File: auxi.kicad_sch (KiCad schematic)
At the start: 45 parts

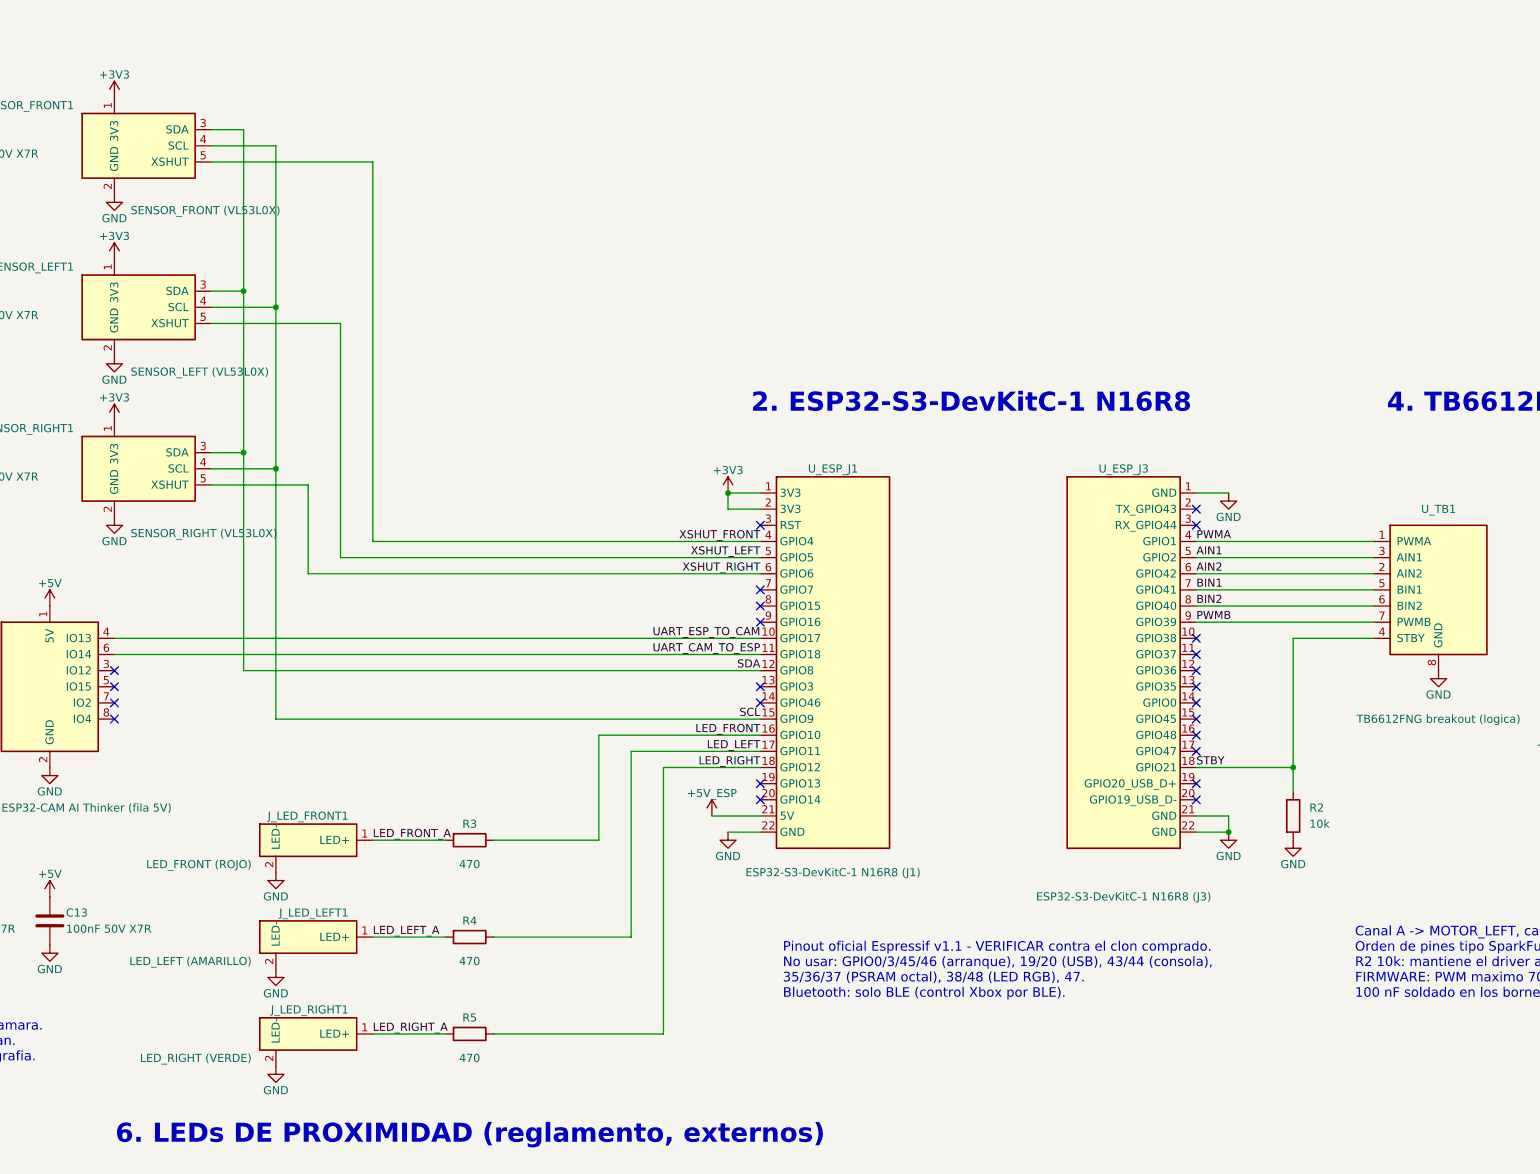
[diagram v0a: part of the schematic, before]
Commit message: feat(pcb): single-layer 110 x 140 mm board with GND pour, soldered from below
Re-do the PCB as a one-copper-layer board for home etching and hand drilling:

- Copper only on B.Cu with a GND pour; F.Cu has no copper (keepout over the
  whole top face). All parts are THT, mounted on top and soldered from below.
  No vias and no jumper wires: no two tracks cross.
- Board outline 110 x 140 mm (was 90 x 100 mm), M3 holes 5 mm from the corners,
  antenna keepouts for the ESP32-S3 and the ESP32-CAM.
- Track width >= 0.4 mm (0.3 mm only between pads / tight bundles), clearance
  0.2 mm, smallest hole 0.3 mm, default via 1.1 / 0.3 mm. Pad diameter = drill
  + 0.8 mm on every pad hole, enforced by auxi.kicad_dru. Four standard
  footprints copied into auxi.pretty with bigger pads.
- GPIOs reassigned so the signals leave the ESP32 headers in the order of their
  destinations (I2C on GPIO4/5, XSHUT 6/7/15, LEDs 8/9/10, motor signals
  reversed on J3). Schematic updated, ERC clean.
- DRC: 0 violations, 0 unconnected items.
- README.md and CLAUDE.md updated; regenerated schematic PDF, BOM, 1:1 print
  PDF (top, copper, mirrored copper) and renders.

Co-Authored-By: Claude Sonnet 5.5 <noreply@anthropic.com>
Claude-Session: https://claude.ai/code/session_01V1Casvb8MJmuQffuKiRczF
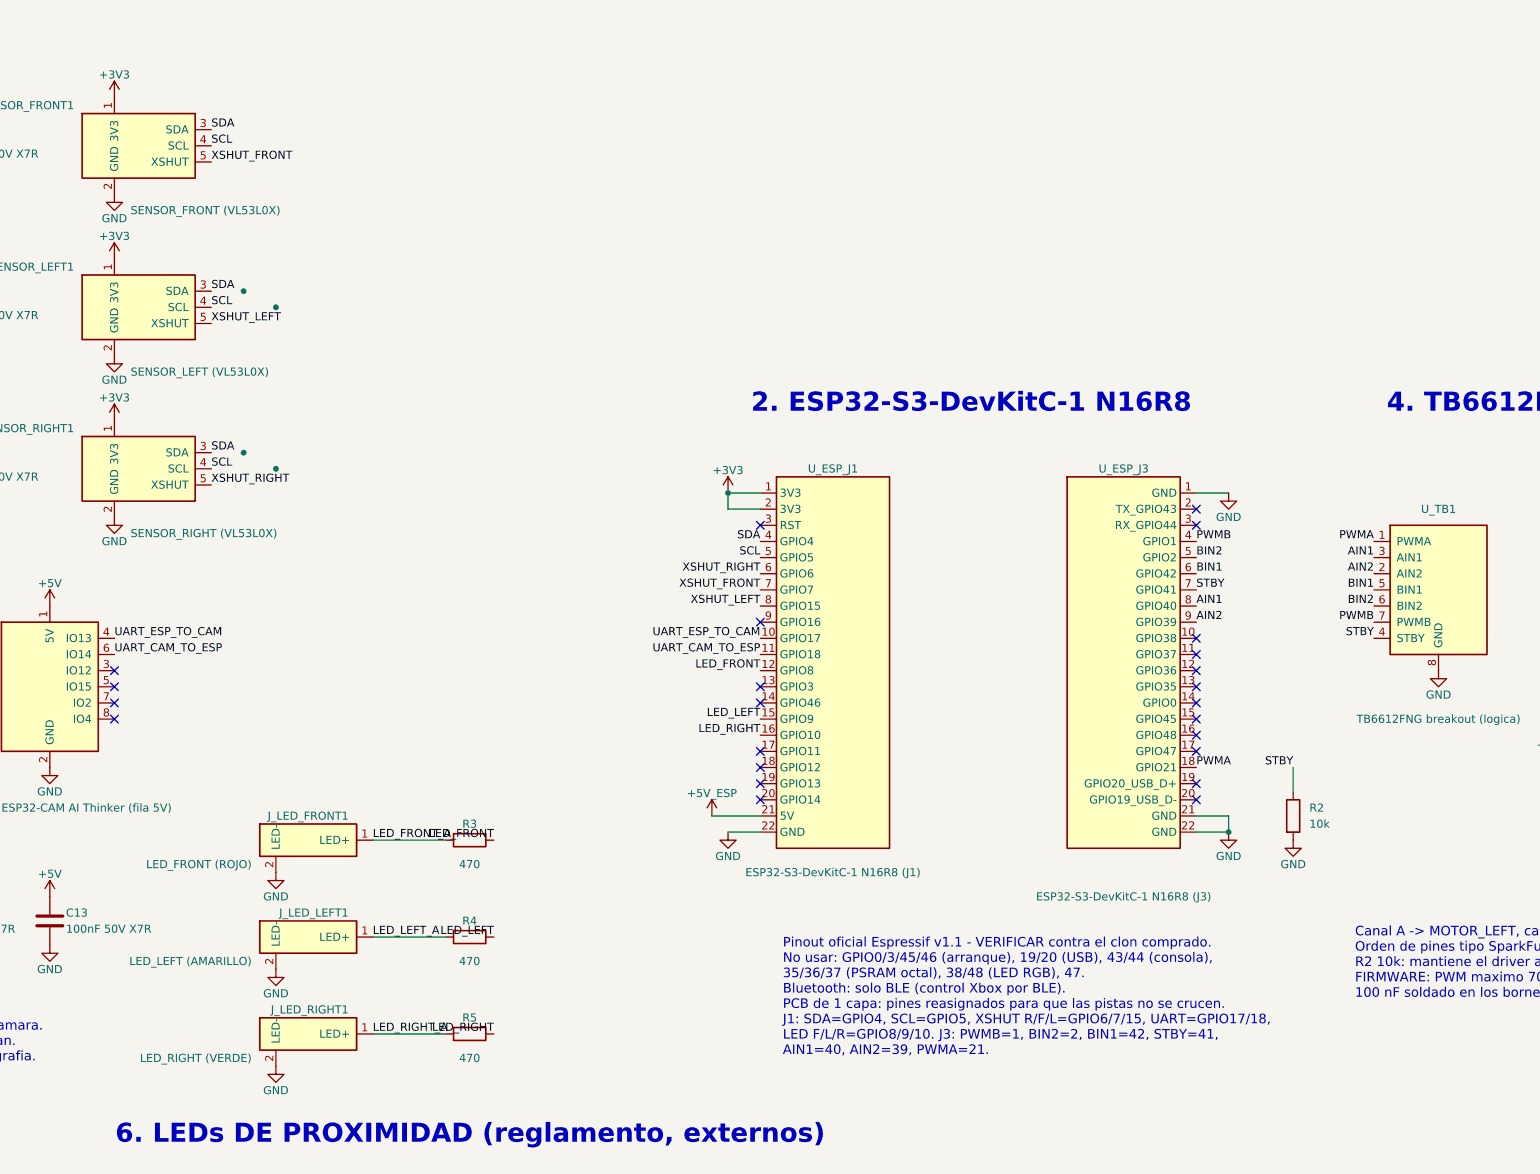
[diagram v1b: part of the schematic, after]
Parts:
- J_LED_FRONT1, J_LED_LEFT1, J_LED_POWER1, J_LED_RIGHT1: footprint Connector_PinHeader_2.54mm:PinHeader_1x02_P2.54mm_Vertical -> auxi:PinHeader_1x02_P2.54mm_Vertical
- J_SENSOR_FRONT1, J_SENSOR_LEFT1, J_SENSOR_RIGHT1: footprint Connector_JST:JST_XH_B5B-XH-A_1x05_P2.50mm_Vertical -> auxi:JST_XH_B5B-XH-A_1x05_P2.50mm_Vertical
- U_CAM1, U_CAM2, U_TB1, U_TB2: footprint Connector_PinSocket_2.54mm:PinSocket_1x08_P2.54mm_Vertical -> auxi:PinSocket_1x08_P2.54mm_Vertical
- U_ESP_J1, U_ESP_J3: footprint Connector_PinSocket_2.54mm:PinSocket_1x22_P2.54mm_Vertical -> auxi:PinSocket_1x22_P2.54mm_Vertical
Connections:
- net AIN1: now also U_ESP_J3.8 (GPIO40); no longer U_ESP_J3.5 (GPIO2)
- net AIN2: now also U_ESP_J3.9 (GPIO39); no longer U_ESP_J3.6 (GPIO42)
- net BIN1: now also U_ESP_J3.6 (GPIO42); no longer U_ESP_J3.7 (GPIO41)
- net BIN2: now also U_ESP_J3.5 (GPIO2); no longer U_ESP_J3.8 (GPIO40)
- net LED_FRONT: now also U_ESP_J1.12 (GPIO8); no longer U_ESP_J1.16 (GPIO10)
- net LED_LEFT: now also U_ESP_J1.15 (GPIO9); no longer U_ESP_J1.17 (GPIO11)
- net LED_RIGHT: now also U_ESP_J1.16 (GPIO10); no longer U_ESP_J1.18 (GPIO12)
- net PWMA: now also U_ESP_J3.18 (GPIO21); no longer U_ESP_J3.4 (GPIO1)
- net PWMB: now also U_ESP_J3.4 (GPIO1); no longer U_ESP_J3.9 (GPIO39)
- net SCL: now also U_ESP_J1.5 (GPIO5); no longer U_ESP_J1.15 (GPIO9)
- net SDA: now also U_ESP_J1.4 (GPIO4); no longer U_ESP_J1.12 (GPIO8)
- net STBY: now also U_ESP_J3.7 (GPIO41); no longer U_ESP_J3.18 (GPIO21)
- net XSHUT_FRONT: now also U_ESP_J1.7 (GPIO7); no longer U_ESP_J1.4 (GPIO4)
- net XSHUT_LEFT: now also U_ESP_J1.8 (GPIO15); no longer U_ESP_J1.5 (GPIO5)
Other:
- note added: "Pinout oficial Espressif v1.1 - VERIFICAR contra el clon comprado. No usar: GPIO0/3/45/46 (arranque), 19/20 (USB), 43/44 (consola), 35/36/37 (PSRAM octal), 38/48 (LED RGB), 47. Bluetooth: solo BLE (control Xbox por BLE). PCB de 1 capa: pines reasignados para que las pistas no se crucen. J1: SDA=GPIO4, SCL=GPIO5, XSHUT R/F/L=GPIO6/7/15, UART=GPIO17/18, LED F/L/R=GPIO8/9/10. J3: PWMB=1, BIN2=2, BIN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"
- note removed: "Pinout oficial Espressif v1.1 - VERIFICAR contra el clon comprado. No usar: GPIO0/3/45/46 (arranque), 19/20 (USB), 43/44 (consola), 35/36/37 (PSRAM octal), 38/48 (LED RGB), 47. Bluetooth: solo BLE (control Xbox por BLE)."

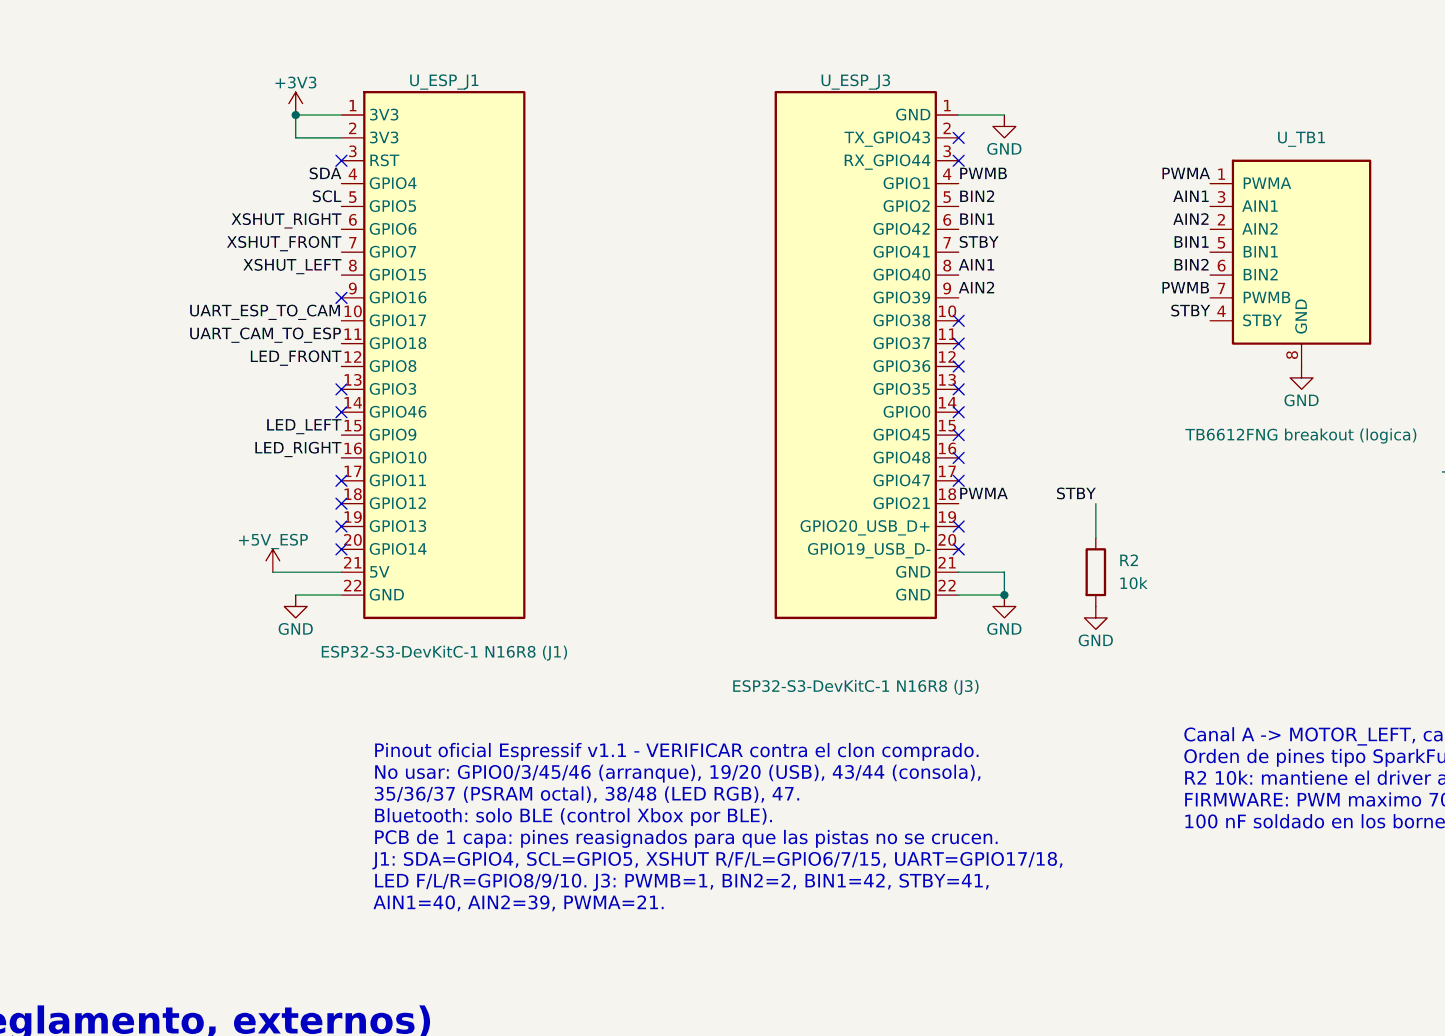
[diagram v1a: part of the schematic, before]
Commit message: Re-layout for the real orientation: 110 mm side is the front, ESP32-S3 USB at the rear edge
- ESP32-CAM at the front-left corner (camera looking forward), sensors
  along the front edge, ESP32-S3 at the rear with the USB end 1 mm from
  the edge, TB6612 and motor terminals on the east side, MP1584 on the
  west side.
- GPIO mapping changed again: XSHUT 4/5/6, SCL 7, SDA 15, UART RX 17 and
  TX 18 (schematic labels updated, ERC clean, PCB nets match the schematic).
- Board re-routed on one layer: 197 tracks, DRC 0 errors, 0 unconnected.
- README, CLAUDE.md, PDFs, renders and DRC report regenerated.

Co-Authored-By: Claude Sonnet 5.5 <noreply@anthropic.com>
Claude-Session: https://claude.ai/code/session_01V1Casvb8MJmuQffuKiRczF
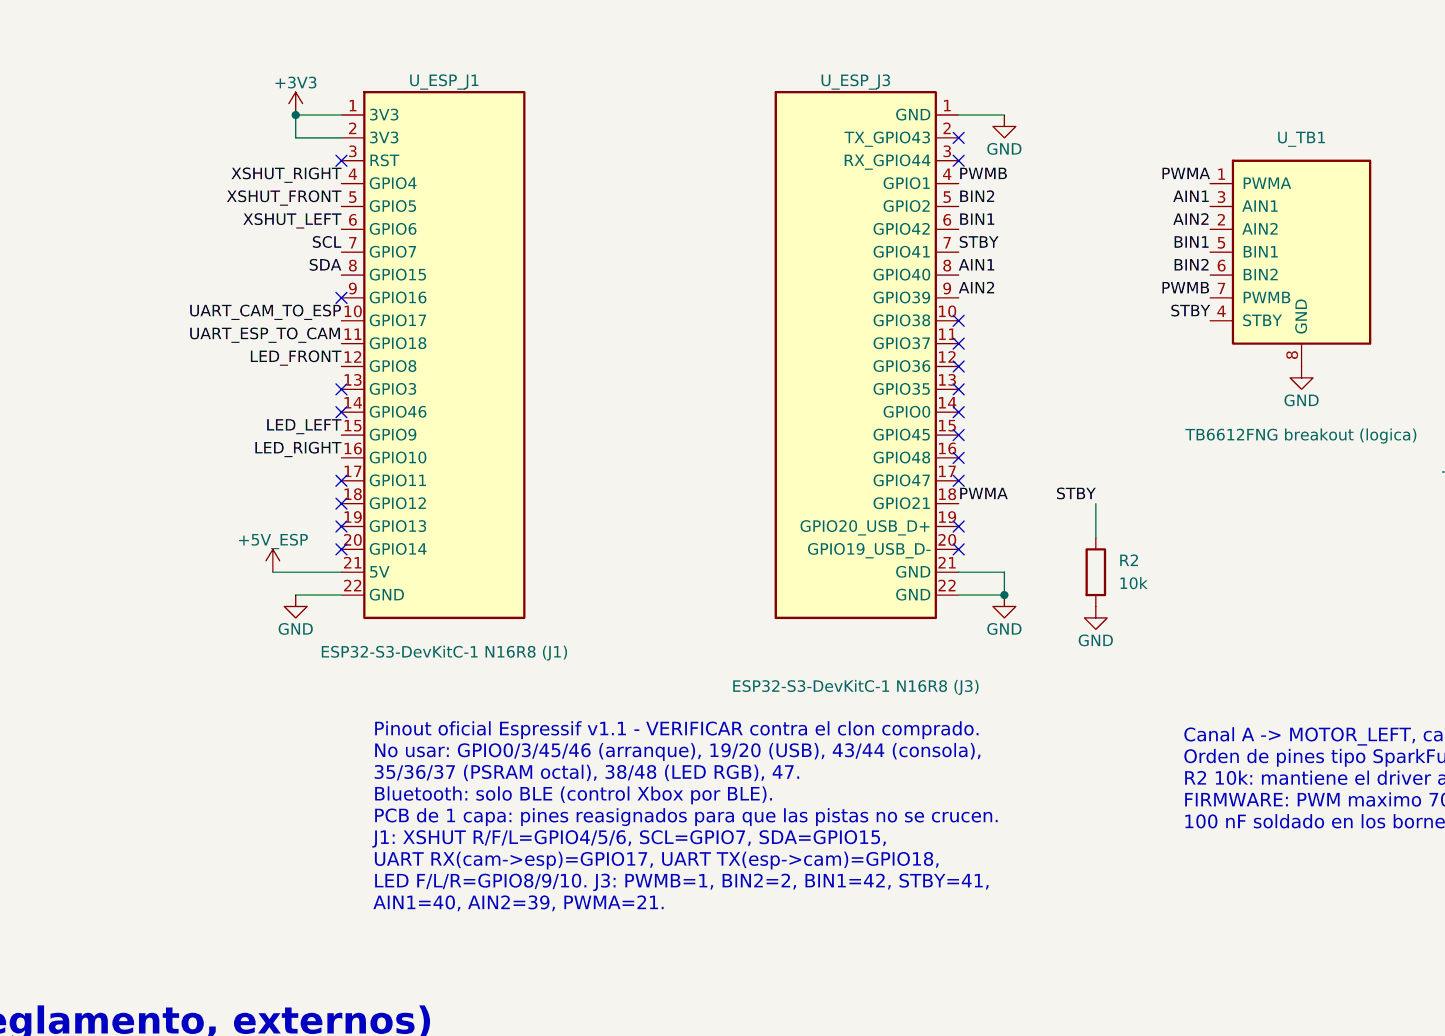
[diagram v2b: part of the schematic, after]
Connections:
- net SCL: now also U_ESP_J1.7 (GPIO7); no longer U_ESP_J1.5 (GPIO5)
- net SDA: now also U_ESP_J1.8 (GPIO15); no longer U_ESP_J1.4 (GPIO4)
- net UART_CAM_TO_ESP: now also U_ESP_J1.10 (GPIO17); no longer U_ESP_J1.11 (GPIO18)
- net UART_ESP_TO_CAM: now also U_ESP_J1.11 (GPIO18); no longer U_ESP_J1.10 (GPIO17)
- net XSHUT_FRONT: now also U_ESP_J1.5 (GPIO5); no longer U_ESP_J1.7 (GPIO7)
- net XSHUT_LEFT: now also U_ESP_J1.6 (GPIO6); no longer U_ESP_J1.8 (GPIO15)
- net XSHUT_RIGHT: now also U_ESP_J1.4 (GPIO4); no longer U_ESP_J1.6 (GPIO6)
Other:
- note added: "Pinout oficial Espressif v1.1 - VERIFICAR contra el clon comprado. No usar: GPIO0/3/45/46 (arranque), 19/20 (USB), 43/44 (consola), 35/36/37 (PSRAM octal), 38/48 (LED RGB), 47. Bluetooth: solo BLE (control Xbox por BLE). PCB de 1 capa: pines reasignados para que las pistas no se crucen. J1: XSHUT R/F/L=GPIO4/5/6, SCL=GPIO7, SDA=GPIO15, UART RX(cam->esp)=GPIO17, UART TX(esp->cam)=GPIO18, LED F/L/R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"
- note removed: "Pinout oficial Espressif v1.1 - VERIFICAR contra el clon comprado. No usar: GPIO0/3/45/46 (arranque), 19/20 (USB), 43/44 (consola), 35/36/37 (PSRAM octal), 38/48 (LED RGB), 47. Bluetooth: solo BLE (control Xbox por BLE). PCB de 1 capa: pines reasignados para que las pistas no se crucen. J1: SDA=GPIO4, SCL=GPIO5, XSHUT R/F/L=GPIO6/7/15, UART=GPIO17/18, LED F/L/R=GPIO8/9/10. J3: PWMB=1, BIN2=2, BIN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"
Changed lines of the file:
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@@
+		)
+	)
+	(label "XSHUT_RIGHT"
+		(at 251.46 107.95 180)
+		(effects
+			(font
+				(size 1.27 1.27)
+			)
+			(justify right bottom)
+		)
+	)
+	(label "XSHUT_FRONT"
+		(at 251.46 110.49 180)
+		(effects
+			(font
+				(size 1.27 1.27)
+			)
+			(justify right bottom)
+		)
+	)
+	(label "XSHUT_LEFT"
+		(at 251.46 113.03 180)
+		(effects
+			(font
+				(size 1.27 1.27)
+			)
+			(justify right bottom)
+		)
+	)
+	(label "SCL"
+		(at 251.46 115.57 180)
+		(effects
+			(font
+				(size 1.27 1.27)
+			)
+			(justify right bottom)
 		)
 	)
 	(label "SDA"
-		(at 251.46 107.95 180)
-		(effects
-			(font
-				(size 1.27 1.27)
-			)
-			(justify right bottom)
-		)
-	)
-	(label "SCL"
-		(at 251.46 110.49 180)
-		(effects
-			(font
-				(size 1.27 1.27)
-			)
-			(justify right bottom)
-		)
-	)
-	(label "XSHUT_RIGHT"
-		(at 251.46 113.03 180)
-		(effects
-			(font
-				(size 1.27 1.27)
-			)
-			(justify right bottom)
-		)
-	)
-	(label "XSHUT_FRONT"
-		(at 251.46 115.57 180)
-		(effects
-			(font
-				(size 1.27 1.27)
-			)
-			(justify right bottom)
-		)
-	)
-	(label "XSHUT_LEFT"
 		(at 251.46 118.11 180)
 		(effects
@@
 		)
 	)
+	(label "UART_CAM_TO_ESP"
+		(at 251.46 123.19 180)
+		(effects
+			(font
+				(size 1.27 1.27)
+			)
+			(justify right bottom)
+		)
+	)
 	(label "UART_ESP_TO_CAM"
-		(at 251.46 123.19 180)
-		(effects
-			(font
-				(size 1.27 1.27)
-			)
-			(justify right bottom)
-		)
-	)
-	(label "UART_CAM_TO_ESP"
 		(at 251.46 125.73 180)
 		(effects
@@
 		)
 	)
-	(text "Pinout oficial Espressif v1.1 - VERIFICAR contra el clon comprado.\nNo usar: GPIO0/3/45/46 (arranque), 19/20 (USB), 43/44 (consola),\n35/36/37 (PSRAM octal), 38/48 (LED RGB), 47.\nBluetooth: solo BLE (control Xbox por BLE).\nPCB de 1 capa: pines reasignados para que las pistas no se crucen.\nJ1: SDA=GPIO4, SCL=GPIO5, XSHUT R/F/L=GPIO6/7/15, UART=GPIO17/18,\nLED F/L/R=GPIO8/9/10. J3: PWMB=1, BIN2=2, BIN1=42, STBY=41,\nAIN1=40, AIN2=39, PWMA=21."
+	(text "Pinout oficial Espressif v1.1 - VERIFICAR contra el clon comprado.\nNo usar: GPIO0/3/45/46 (arranque), 19/20 (USB), 43/44 (consola),\n35/36/37 (PSRAM octal), 38/48 (LED RGB), 47.\nBluetooth: solo BLE (control Xbox por BLE).\nPCB de 1 capa: pines reasignados para que las pistas no se crucen.\nJ1: XSHUT R/F/L=GPIO4/5/6, SCL=GPIO7, SDA=GPIO15,\nUART RX(cam->esp)=GPIO17, UART TX(esp->cam)=GPIO18,\nLED F/L/R=GPIO8/9/10. J3: PWMB=1, BIN2=2, BIN1=42, STBY=41,\nAIN1=40, AIN2=39, PWMA=21."
 		(exclude_from_sim no)
 		(at 255 189.00 0)
